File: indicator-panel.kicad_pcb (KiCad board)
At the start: 2 copper layers, 133.1 x 77.2 mm, 83 parts, among them J101 Power In (+12V), J102 GND, J103 GND, P101 Data in, P102 Data Out, P103 Power, P104 Power, U101 MAX3094E, U102 STP16CP05, U103 STP16CP05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

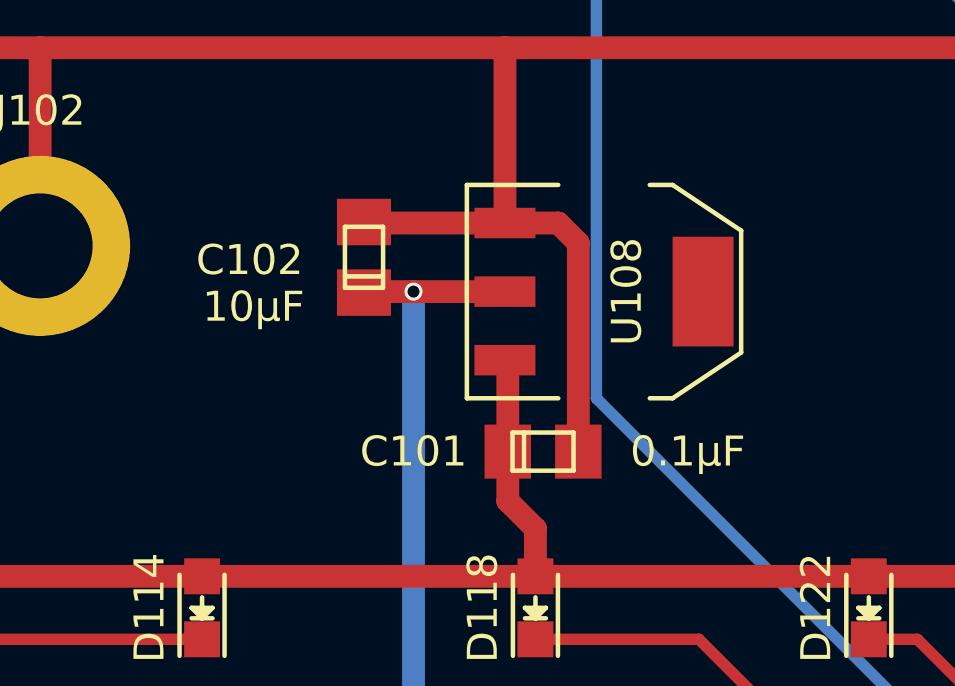
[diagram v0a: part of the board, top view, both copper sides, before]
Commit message: Changed the tantalum capacitor footprint to more clearly show the positive end. Added some text around the power connector on the back.
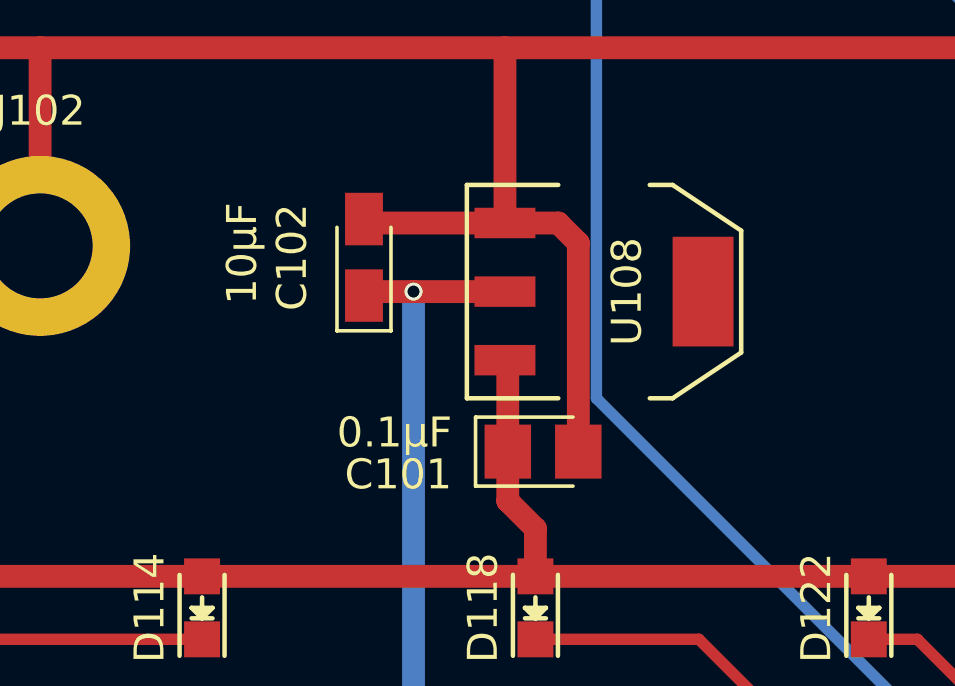
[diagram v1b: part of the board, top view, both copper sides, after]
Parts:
- added REF**: Barrel, Barrel, B.Cu at (128.8, 80.9)
- C101: footprint Capacitors_Tantalum_SMD:TantalC_SizeR_EIA-2012 -> Capacitors_Tantalum_SMD:CP_Tantalum_Case-R_EIA-2012-12_Reflow
- C102: footprint Capacitors_Tantalum_SMD:TantalC_SizeR_EIA-2012 -> Capacitors_Tantalum_SMD:CP_Tantalum_Case-R_EIA-2012-12_Wave
- J101: value Power In (+12V) -> Power In (5 - 12V); footprint PJ-032B -> myMods.pretty:PJ-032B
- turned C101 to 0 degrees
- turned C102 to 90 degrees
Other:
- board text added: "2.5 x 5.5mm"

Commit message: tweaks
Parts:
- removed REF** (x2): MountingHole_3-5mm, Mounting_Holes:MountingHole_3-5mm
- added H101: MountingHole, MountingHole:MountingHole_3.5mm, F.Cu at (89.4, 118.4)
- added H102: MountingHole, MountingHole:MountingHole_3.5mm, F.Cu at (156.7, 118.4)
- FID1, FID2, FID3, FID4: footprint Fiducials:Fiducial_1mm_Dia_2.54mm_Outer_CopperTop -> Fiducial:Fiducial_1mm_Mask2mm
- J101: footprint myMods.pretty:PJ-032B -> myMods:PJ-032B
- PowerLogo1: renamed from REF**; value Barrel -> Power Logo; footprint Barrel -> myMods:Barrel
- moved PowerLogo1 16.8 mm to (142.7, 90.2)
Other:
- board text added: "Vintage Computer Engineering Indicator Panel IP101 v 2.1 2020-11-18"
- board text removed: "Vintage Computer Engineering Indicator Panel IP101 v 2.0 2018-02-23"
